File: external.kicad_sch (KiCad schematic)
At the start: 22 parts

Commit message: v1
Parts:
- added J3, J4: 2157601003, CONN03_2157601003_MOL, symbol 3pinmolex:2157601003
- added unit 7 of U3
- added unit 7 of U4
- added unit 7 of U5
- added unit 7 of U6
- added unit 7 of U7
- gave numbers to parts that had none: 22
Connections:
- net +3V3: now also U3.14 (VCC), U4.14 (VCC), U5.14 (VCC), U6.14 (VCC), U7.14 (VCC)
- net GND: now also J3.1, J4.1, U3.7 (GND), U4.7 (GND), U5.7 (GND), U6.7 (GND), U7.7 (GND)
- new net +5V: J3.2, J4.2
- new net LED: J4.3
- new net MIST: J3.3
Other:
- note added: "Connectors"
- moved on the sheet: C14, C15, C16, C17, C18, J2, R11, R12, R13, R14, R15, R16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

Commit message: v2
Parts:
- removed U4, U5, U6, U7: 74HC14, symbol 74xx:74HC14
- added unit 5 of U3
- added unit 4 of U3
- added unit 2 of U3
- added unit 3 of U3
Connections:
- net A: now also U3.6
- net B: now also U3.4
- net C: now also U3.10
- net D: now also U3.8
- net at C18.1, R20.1: now also U3.11
- net at C16.1, R16.1: now also U3.5
- net at C17.1, R18.1: now also U3.9
- net at C15.1, R13.1: now also U3.3
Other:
- moved on the sheet: U3G

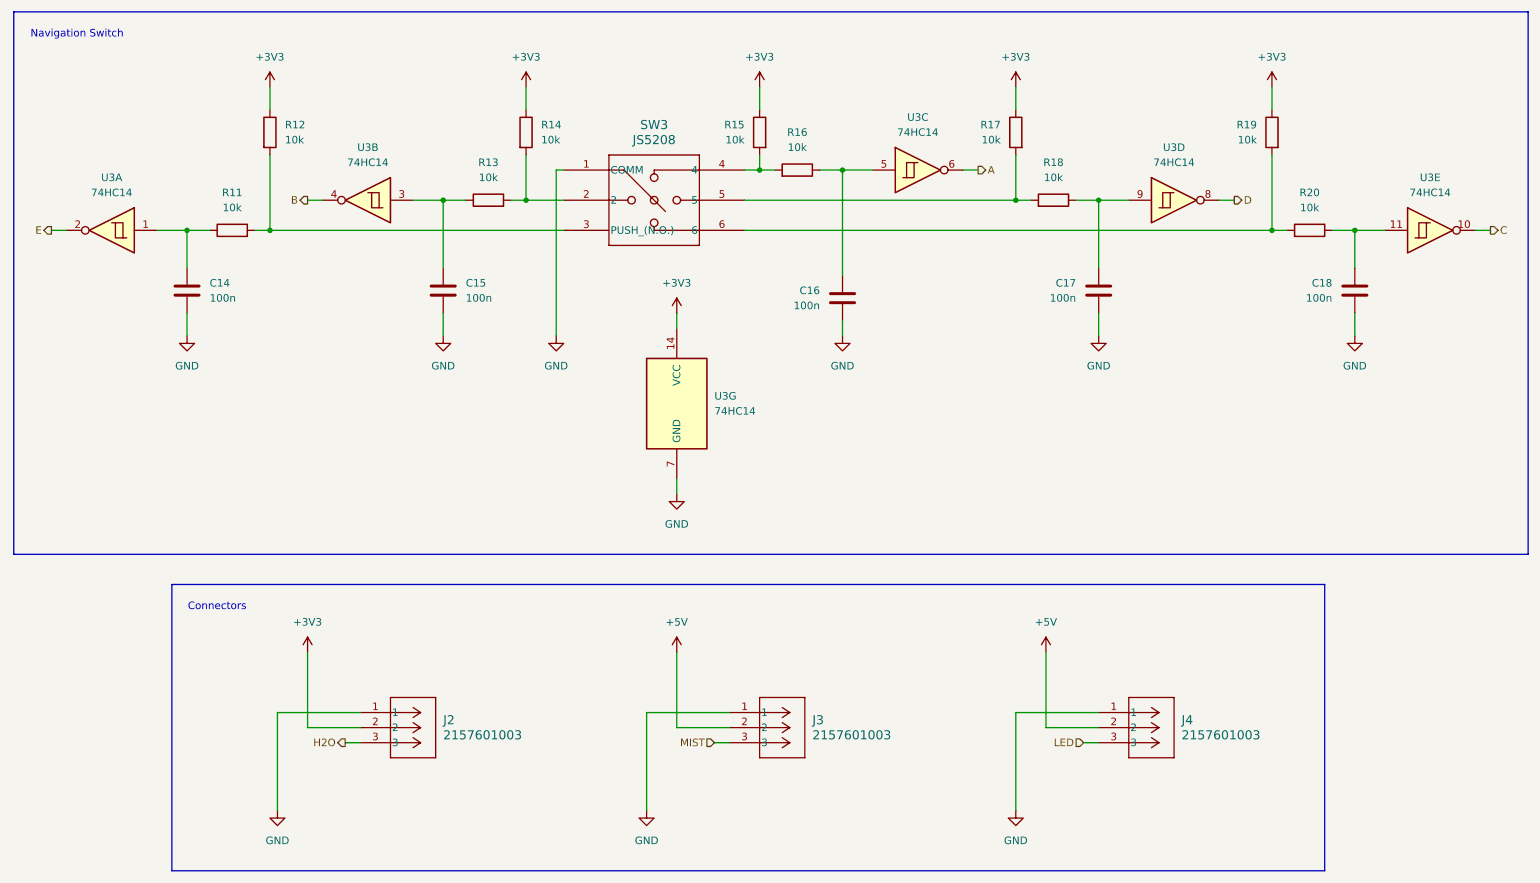
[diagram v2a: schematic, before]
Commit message: passed drc (somehow)
board routing is def cooked
verify:
- boost layout
- usb terminal layout
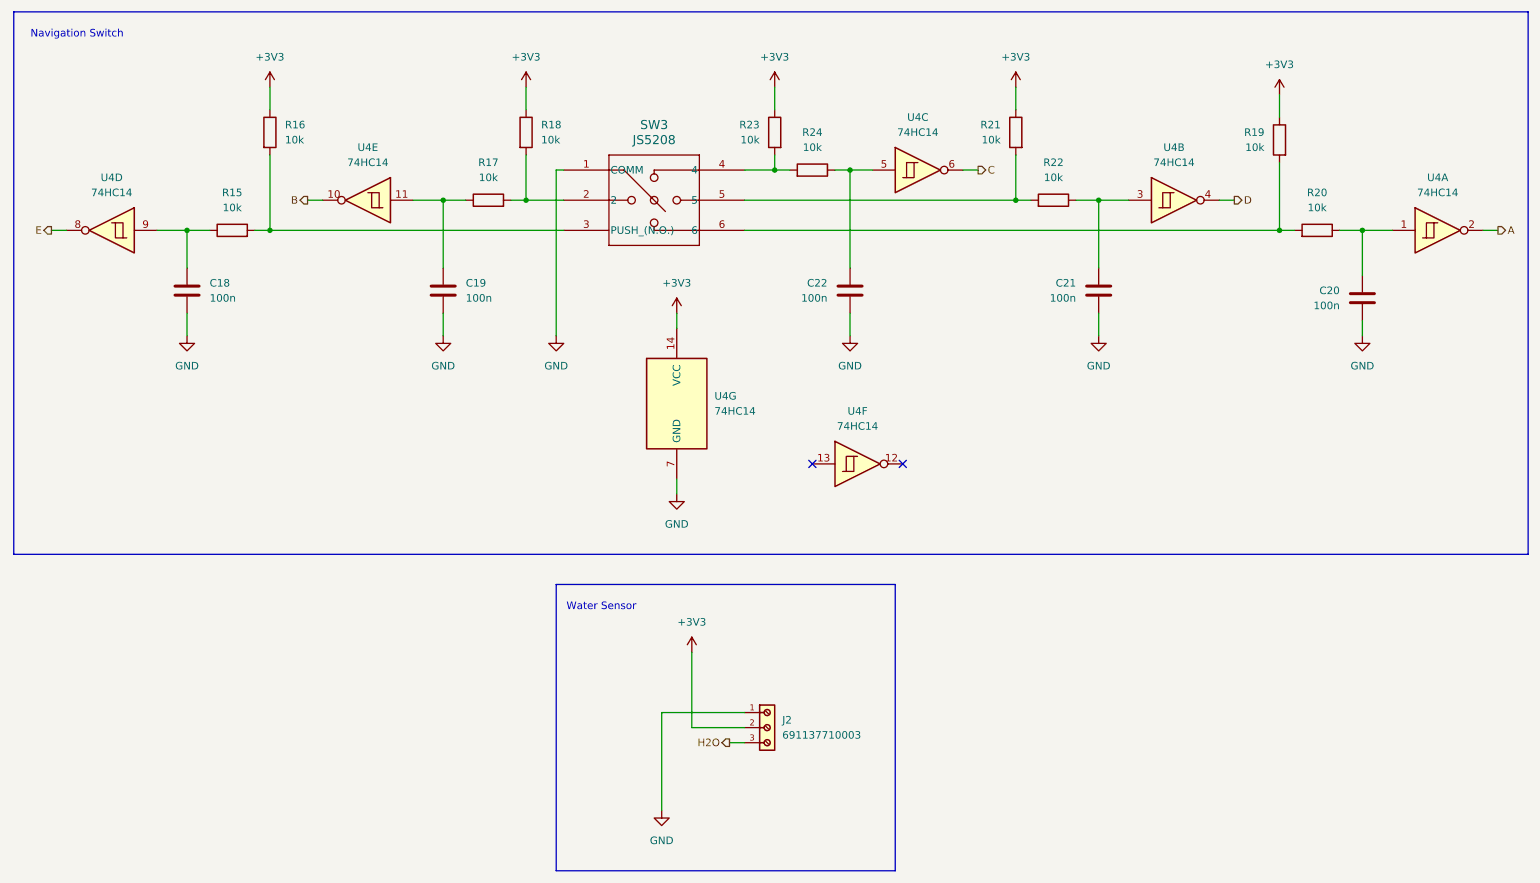
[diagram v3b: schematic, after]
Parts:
- removed J2, J3, J4: 2157601003, CONN03_2157601003_MOL, symbol 3pinmolex:2157601003
- added J2: 691137710003, footprints:691137710003, symbol 691137710003:691137710003
- added unit 6 of U4
- C18: renamed from C14; footprint (none) -> Capacitor_SMD:C_0603_1608Metric_Pad1.08x0.95mm_HandSolder
- C19: renamed from C15; footprint (none) -> Capacitor_SMD:C_0603_1608Metric_Pad1.08x0.95mm_HandSolder
- C20: renamed from C16; footprint (none) -> Capacitor_SMD:C_0603_1608Metric_Pad1.08x0.95mm_HandSolder
- C21: renamed from C17; footprint (none) -> Capacitor_SMD:C_0603_1608Metric_Pad1.08x0.95mm_HandSolder
- C22: renamed from C18; footprint (none) -> Capacitor_SMD:C_0603_1608Metric_Pad1.08x0.95mm_HandSolder
- R15: renamed from R11; footprint (none) -> Resistor_SMD:R_0603_1608Metric
- R16: renamed from R12; footprint (none) -> Resistor_SMD:R_0603_1608Metric
- R17: renamed from R13; footprint (none) -> Resistor_SMD:R_0603_1608Metric
- R18: renamed from R14; footprint (none) -> Resistor_SMD:R_0603_1608Metric
- R19: renamed from R15; footprint (none) -> Resistor_SMD:R_0603_1608Metric
- R20: renamed from R16; footprint (none) -> Resistor_SMD:R_0603_1608Metric
- R21: renamed from R17; footprint (none) -> Resistor_SMD:R_0603_1608Metric
- R22: renamed from R18; footprint (none) -> Resistor_SMD:R_0603_1608Metric
- R23: renamed from R19; footprint (none) -> Resistor_SMD:R_0603_1608Metric
- R24: renamed from R20; footprint (none) -> Resistor_SMD:R_0603_1608Metric
- SW3: footprint SW6_JS5208_ESW -> footprints:SW_JS5208
- U4: renamed from U3; footprint (none) -> Package_DIP:DIP-14_W7.62mm
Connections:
- net +3V3: now also J2.2
- net A: now also U4.2; no longer U4.6
- net B: now also U4.10; no longer U4.4
- net C: now also U4.6; no longer U4.10
- net D: now also U4.4; no longer U4.8
- net E: now also U4.8; no longer U4.2
- net GND: now also J2.1
- net H2O: now also J2.3
- net at C20.1, R20.1: now also U4.1; no longer U4.5
- net at R19.2, R20.2: now also SW3.6; no longer SW3.4
- net at C22.1, R24.1: now also U4.5; no longer U4.11
- net at C21.1, R22.1: now also U4.3; no longer U4.9
- net at C18.1, R15.1: now also U4.9; no longer U4.1
- net at C19.1, R17.1: now also U4.11; no longer U4.3
- net at R23.2, R24.2: now also SW3.4; no longer SW3.6
- no-connect marks 0 -> 2
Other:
- note added: "Water Sensor"
- note removed: "Connectors"
- moved on the sheet: C20, C22, R19, R20, R23, R24, U4A, U4B, U4D, U4E
